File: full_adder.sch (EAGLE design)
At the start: 90 parts, among them U1001 FDS6892A, U1002 FDS6892A, U1003 FDS6892A, U101 ATTINY45-20P, U201 CD4052BE, U202 CD4052BE, U203 CD4052BE, U401 KM28C65A-20, U501 74HC4051N,652, U601 NE555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

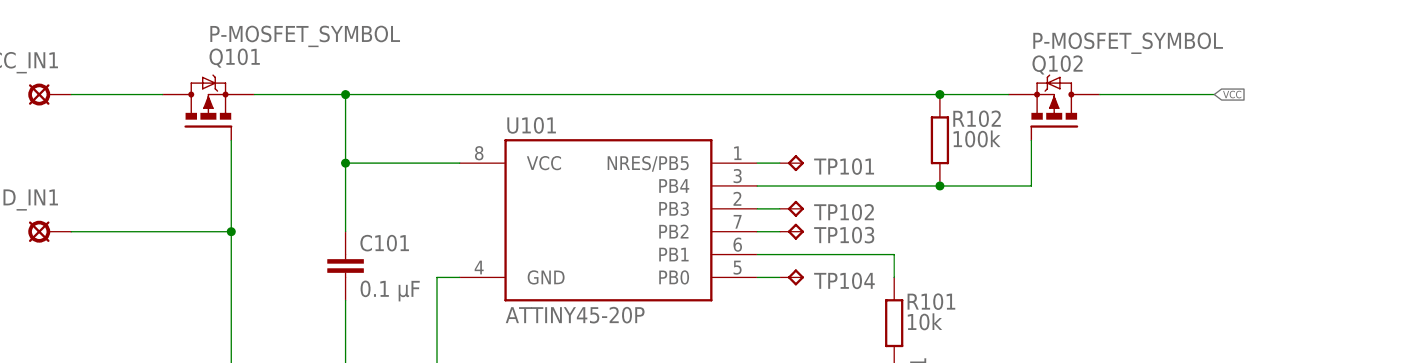
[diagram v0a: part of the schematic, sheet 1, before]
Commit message: p-channel footprint
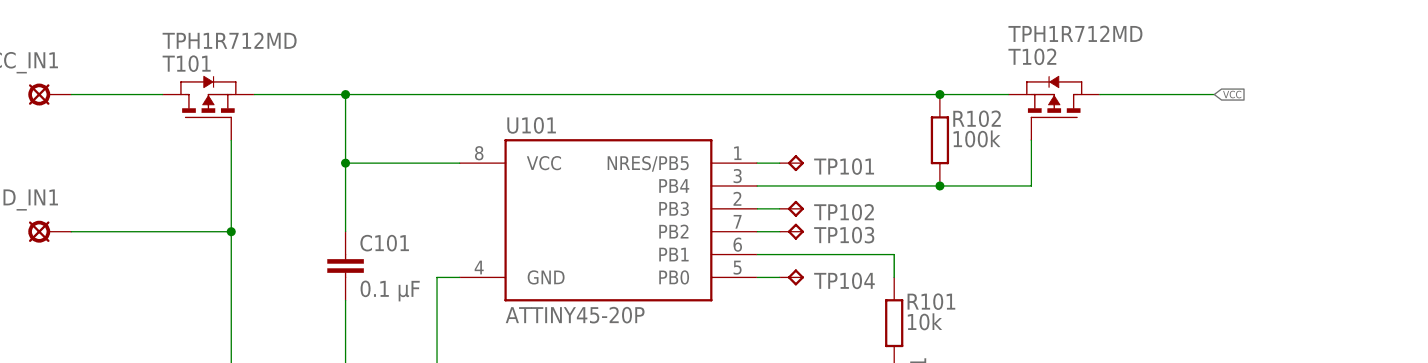
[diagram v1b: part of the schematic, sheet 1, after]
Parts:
- added T101, T102: TPH1R712MD, SamacSys_Parts:TPH1R712MD
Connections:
- net GND: now also T101.G
- net N$41: now also T101.D
- net N$42: now also T101.S, T102.S
- net N$43: now also T102.G
- net VCC: now also T102.D
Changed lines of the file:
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@@
 <part name="GND_IN1" library="solpad" library_urn="urn:adsk.eagle:library:364" deviceset="LSP11" device="" package3d_urn="urn:adsk.eagle:package:26502/1"/>
 <part name="GND40" library="supply1" library_urn="urn:adsk.eagle:library:371" deviceset="GND" device=""/>
-<part name="Q101" library="transistor-power" library_urn="urn:adsk.eagle:library:400" deviceset="P-MOSFET_SYMBOL" device=""/>
 <part name="U101" library="_hhn_attiny25_45_85" deviceset="ATTINY45*" device="P" technology="-20"/>
 <part name="GND52" library="supply1" library_urn="urn:adsk.eagle:library:371" deviceset="GND" device=""/>
@@
 <part name="TP103" library="testpad" library_urn="urn:adsk.eagle:library:385" deviceset="TP" device="B2,54" package3d_urn="urn:adsk.eagle:package:27948/1"/>
 <part name="TP104" library="testpad" library_urn="urn:adsk.eagle:library:385" deviceset="TP" device="B2,54" package3d_urn="urn:adsk.eagle:package:27948/1"/>
-<part name="Q102" library="transistor-power" library_urn="urn:adsk.eagle:library:400" deviceset="P-MOSFET_SYMBOL" device=""/>
+<part name="T102" library="SamacSys_Parts" deviceset="TPH1R712MD" device=""/>
+<part name="T101" library="SamacSys_Parts" deviceset="TPH1R712MD" device=""/>
 </parts>
 <sheets>
@@
 <attribute name="VALUE" x="307.34" y="180.34" size="1.778" layer="96"/>
 </instance>
-<instance part="Q101" gate="G$1" x="307.34" y="220.98" smashed="yes" rot="MR90">
-<attribute name="NAME" x="307.34" y="228.6" size="1.778" layer="95" rot="MR180"/>
-<attribute name="VALUE" x="307.34" y="231.14" size="1.778" layer="96" rot="MR180"/>
-</instance>
 <instance part="U101" gate="G$1" x="350.52" y="210.82" smashed="yes">
 <attribute name="NAME" x="340.36" y="219.202" size="1.778" layer="95"/>
@@
 <attribute name="TP_SIGNAL_NAME" x="372.11" y="201.93" size="1.778" layer="97" rot="R270"/>
 </instance>
-<instance part="Q102" gate="G$1" x="401.32" y="220.98" smashed="yes" rot="R90">
-<attribute name="NAME" x="398.78" y="226.06" size="1.778" layer="95"/>
-<attribute name="VALUE" x="398.78" y="228.6" size="1.778" layer="96"/>
+<instance part="T102" gate="G$1" x="401.32" y="223.52" smashed="yes" rot="MR90">
+<attribute name="VALUE" x="396.24" y="231.14" size="1.778" layer="96" rot="MR180"/>
+<attribute name="NAME" x="396.24" y="228.6" size="1.778" layer="95" rot="MR180"/>
+</instance>
+<instance part="T101" gate="G$1" x="307.34" y="223.52" smashed="yes" rot="R90">
+<attribute name="VALUE" x="302.26" y="228.6" size="1.778" layer="96"/>
+<attribute name="NAME" x="302.26" y="226.06" size="1.778" layer="95"/>
 </instance>
 </instances>
@@
 <wire x1="406.4" y1="223.52" x2="419.1" y2="223.52" width="0.1524" layer="91"/>
 <label x="419.1" y="223.52" size="0.8128" layer="95" xref="yes"/>
+<pinref part="T102" gate="G$1" pin="D"/>
 </segment>
 </net>
@@
 <segment>
 <pinref part="GND_IN1" gate="1" pin="MP"/>
-<wire x1="309.88" y1="218.44" x2="309.88" y2="208.28" width="0.1524" layer="91"/>
 <wire x1="309.88" y1="208.28" x2="292.1" y2="208.28" width="0.1524" layer="91"/>
 <pinref part="GND40" gate="1" pin="GND"/>
 <wire x1="309.88" y1="185.42" x2="309.88" y2="208.28" width="0.1524" layer="91"/>
+<pinref part="T101" gate="G$1" pin="G"/>
+<wire x1="309.88" y1="218.44" x2="309.88" y2="208.28" width="0.1524" layer="91"/>
 <junction x="309.88" y="208.28"/>
 </segment>
@@
 </segment>
 </net>
-<net name="N$41" class="0">
-<segment>
-<pinref part="VCC_IN1" gate="1" pin="MP"/>
-<wire x1="292.1" y1="223.52" x2="302.26" y2="223.52" width="0.1524" layer="91"/>
-</segment>
-</net>
 <net name="N$42" class="0">
 <segment>
-<wire x1="312.42" y1="223.52" x2="322.58" y2="223.52" width="0.1524" layer="91"/>
 <pinref part="U101" gate="G$1" pin="VCC"/>
 <wire x1="322.58" y1="223.52" x2="322.58" y2="215.9" width="0.1524" layer="91"/>
 <wire x1="322.58" y1="215.9" x2="335.28" y2="215.9" width="0.1524" layer="91"/>
 <wire x1="322.58" y1="223.52" x2="388.62" y2="223.52" width="0.1524" layer="91"/>
-<junction x="322.58" y="223.52"/>
 <pinref part="C101" gate="G$1" pin="1"/>
 <wire x1="388.62" y1="223.52" x2="396.24" y2="223.52" width="0.1524" layer="91"/>
@@
 <pinref part="R102" gate="G$1" pin="2"/>
 <junction x="388.62" y="223.52"/>
+<pinref part="T101" gate="G$1" pin="S"/>
+<wire x1="312.42" y1="223.52" x2="322.58" y2="223.52" width="0.1524" layer="91"/>
+<junction x="322.58" y="223.52"/>
+<pinref part="T102" gate="G$1" pin="S"/>
 </segment>
 </net>
@@
 <pinref part="R102" gate="G$1" pin="1"/>
 <junction x="388.62" y="213.36"/>
+<pinref part="T102" gate="G$1" pin="G"/>
 </segment>
 </net>
@@
 </segment>
 </net>
+<net name="N$41" class="0">
+<segment>
+<pinref part="VCC_IN1" gate="1" pin="MP"/>
+<pinref part="T101" gate="G$1" pin="D"/>
+<wire x1="292.1" y1="223.52" x2="302.26" y2="223.52" width="0.1524" layer="91"/>
+</segment>
+</net>

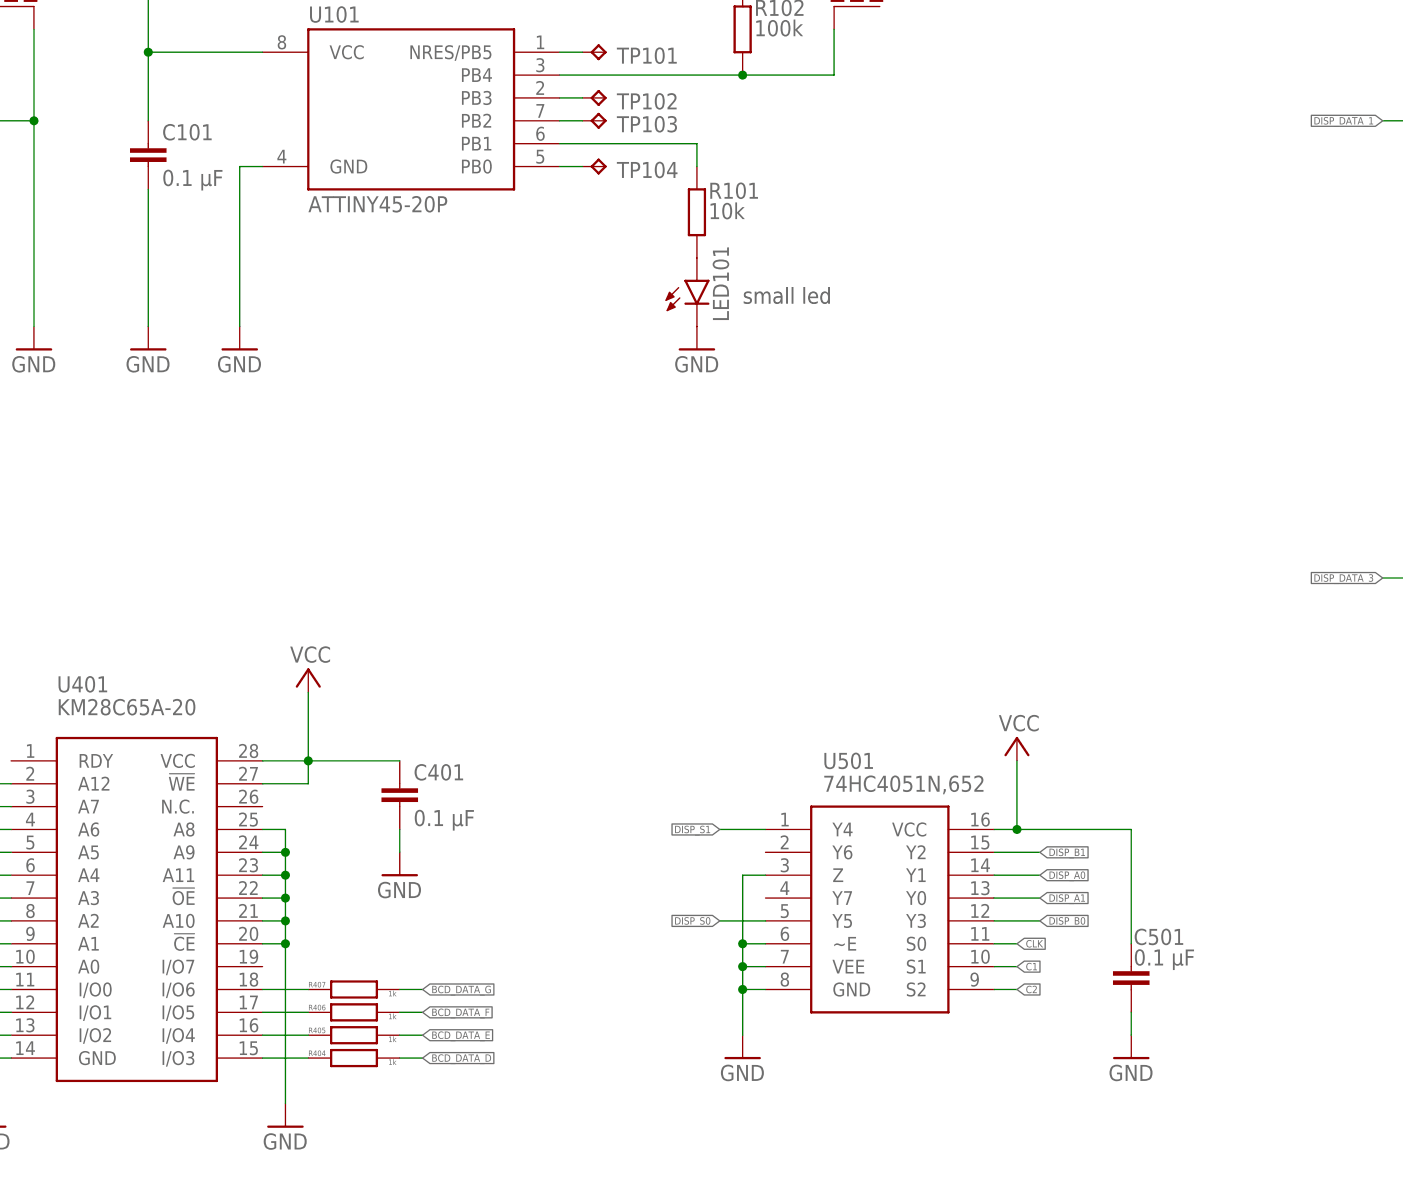
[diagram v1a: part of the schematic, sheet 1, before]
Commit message: swapped capacitor footprints
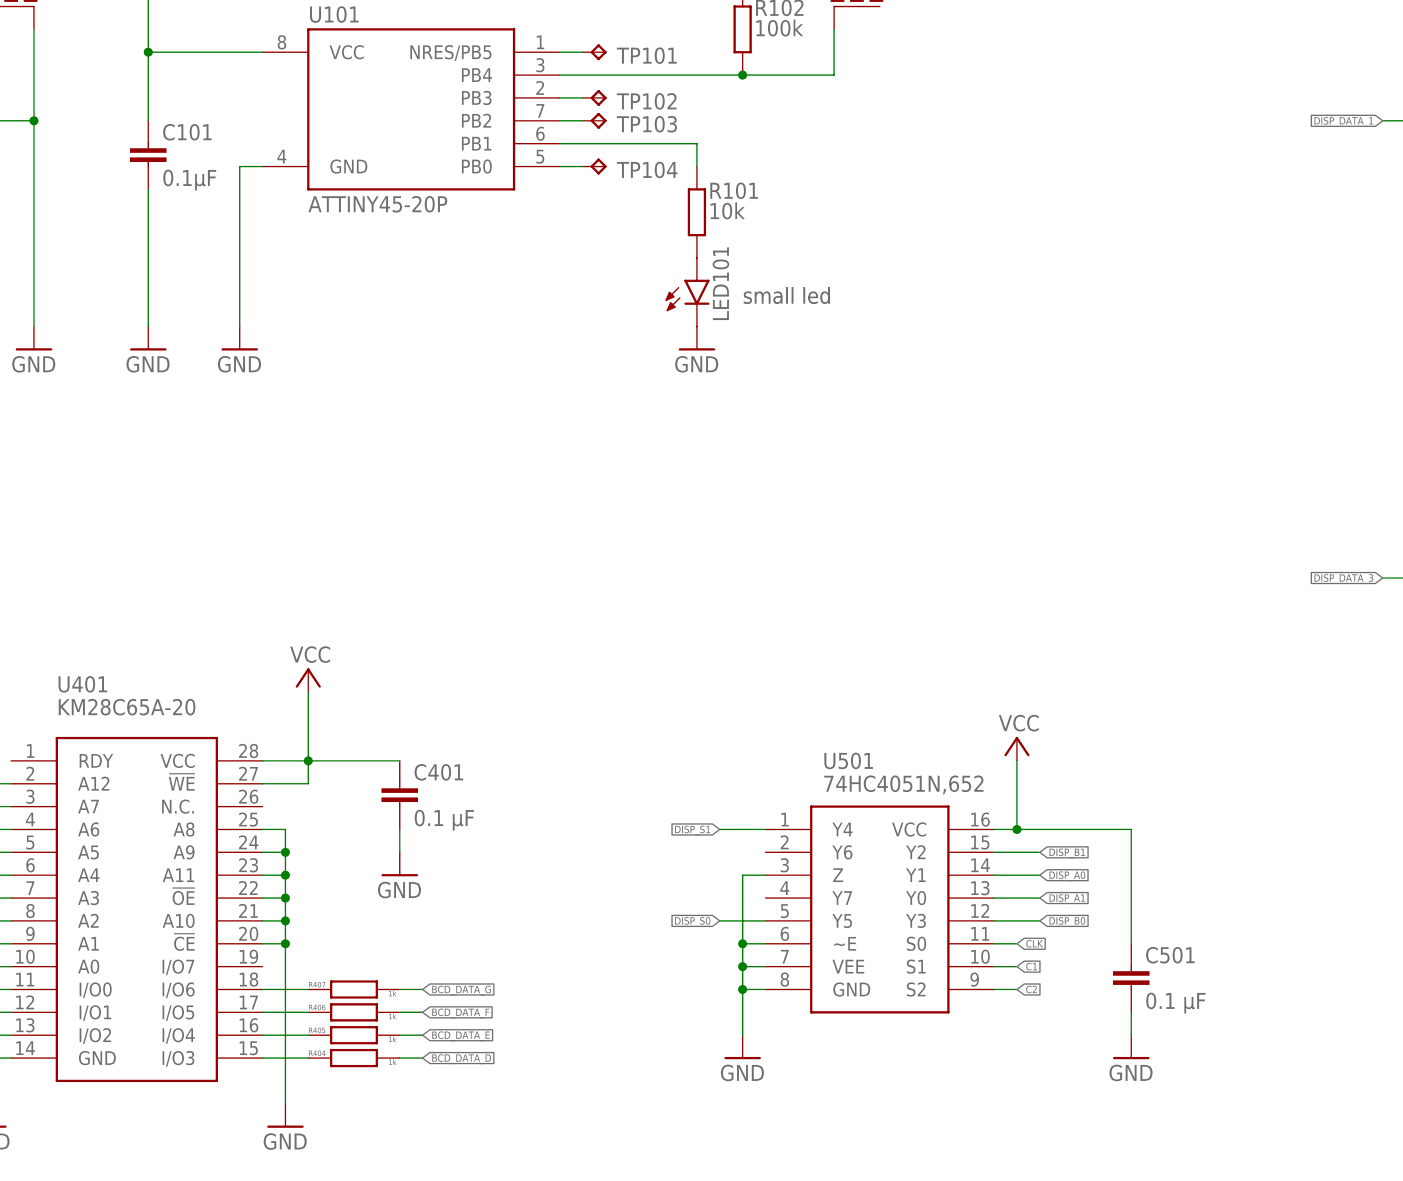
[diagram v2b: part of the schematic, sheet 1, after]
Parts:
- C101: value 0.1 µF -> 0.1µF; device rcl:C-EU025-024X044 -> rcl:C-EUC1206
- C201, C202, C203, C301, C302, C303, C304, C305, C401, C501, C601, C602, C603, C701: device rcl:C-EU025-024X044 -> rcl:C-EUC1206

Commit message: poti test pads
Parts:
- added POT_IN, POT_OUT, TP1: TPB2,54, testpad:TPB2,54
- C101: value 0.1µF -> 0.1 µF; device rcl:C-EUC1206 -> rcl:C-EU025-024X044
- C201, C202, C203, C301, C302, C303, C304, C305, C401, C501, C601, C602, C603, C701: device rcl:C-EUC1206 -> rcl:C-EU025-024X044
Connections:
- net N$14: now also POT_OUT.TP
- net N$15: now also POT_IN.TP
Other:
- moved on the sheet: R603

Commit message: fixed chaos
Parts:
- removed TP1: TPB2,54, testpad:TPB2,54
- C101: value 0.1 µF -> 0.1µF; device rcl:C-EU025-024X044 -> rcl:C-EUC1206
- C201, C202, C203, C301, C302, C303, C304, C305, C401, C501, C603, C701: device rcl:C-EU025-024X044 -> rcl:C-EUC1206
- C601: value 1 µF -> 1µF; device rcl:C-EU025-024X044 -> rcl:C-EU050-024X044
- C602: value 0.01 µF -> 0.01µF; device rcl:C-EU025-024X044 -> rcl:C-EU050-024X044
- renumbered POT_IN to POT_TP1, POT_OUT to POT_TP2

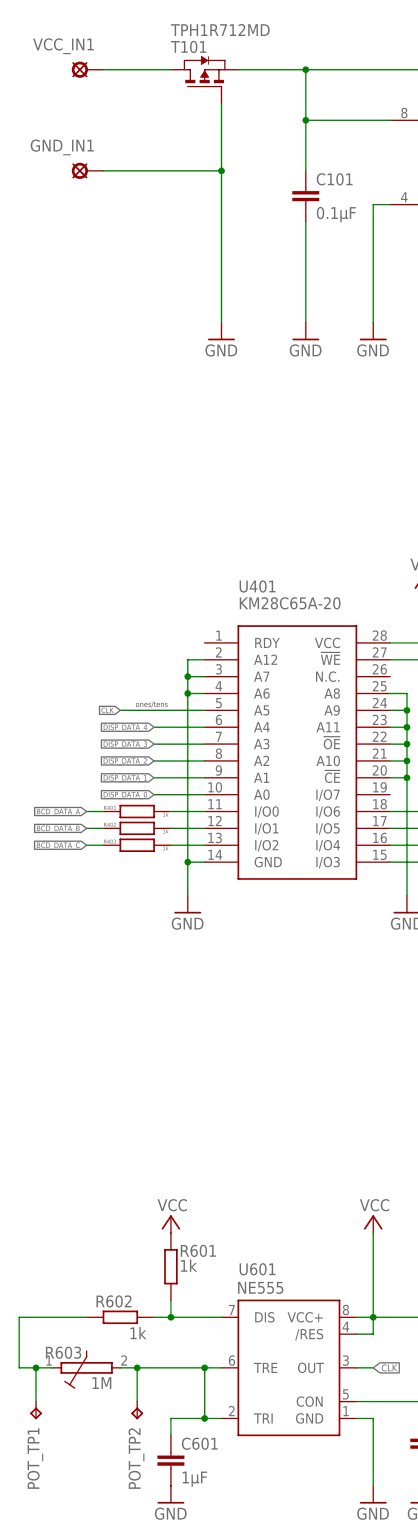
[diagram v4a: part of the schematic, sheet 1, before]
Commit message: swapped led footprints
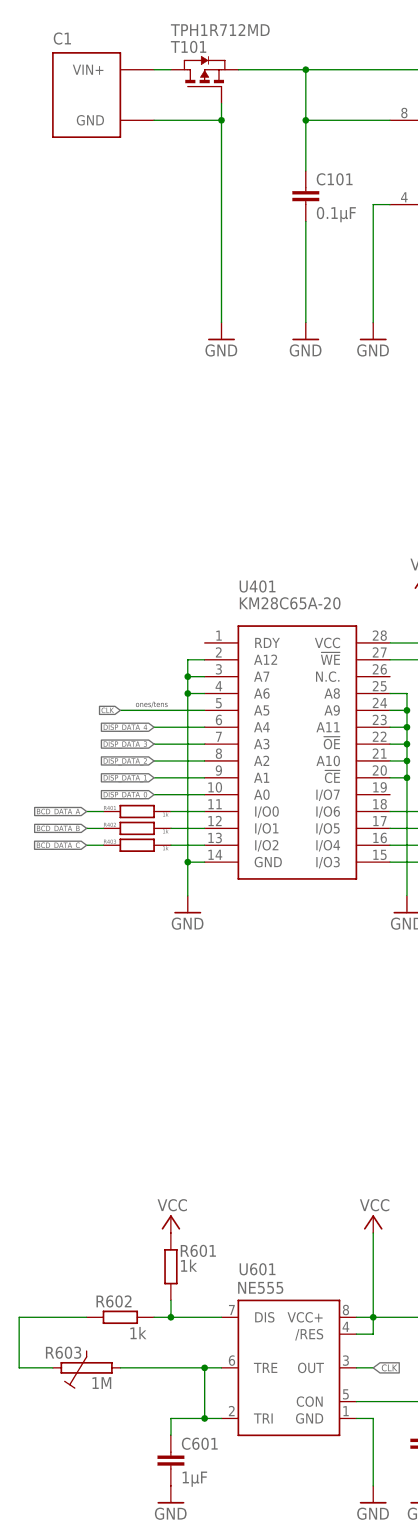
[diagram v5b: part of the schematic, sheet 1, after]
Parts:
- removed GND_IN1, VCC_IN1: LSP11, solpad:LSP11
- removed POT_TP1, POT_TP2: TPB2,54, testpad:TPB2,54
- added C1: BATTERY_CONNECTOR, custom:BATTERY_CONNECTOR
- LED1001, LED1002, LED1003, LED1004, LED1005, LED101, LED1101, LED1102, LED1103, LED1104, LED1105, LED1106, LED1107, LED1108: device led:LED5MM -> led:LED3MM
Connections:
- net GND: now also C1.GND; no longer GND_IN1.MP
- net N$14: no longer POT_TP2.TP
- net N$15: no longer POT_TP1.TP
- net N$41: now also C1.VIN+; no longer VCC_IN1.MP

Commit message: Components placed
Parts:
- U101: value ATTINY45-20P -> ATTINY85
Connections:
- new net N$45: R401.2, U401.I/O0
- new net N$46: R402.2, U401.I/O1
- new net N$47: R403.2, U401.I/O2
- new net N$48: R407.1, U401.I/O6
- new net N$49: R406.1, U401.I/O5
- new net N$50: R405.1, U401.I/O4
- new net N$51: R404.1, U401.I/O3
- net BCD_DATA_A: no longer R401.2, U401.I/O0
- net BCD_DATA_B: no longer R402.2, U401.I/O1
- net BCD_DATA_C: no longer R403.2, U401.I/O2
- net BCD_DATA_D: no longer R404.1, U401.I/O3
- net BCD_DATA_E: no longer R405.1, U401.I/O4
- net BCD_DATA_F: no longer R406.1, U401.I/O5
- net BCD_DATA_G: no longer R407.1, U401.I/O6

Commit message: routing v1 done
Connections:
- new net N$52: U701.1!Q, U701.1D
- net C1: no longer U701.1!Q, U701.1D
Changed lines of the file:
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@@
 <net name="C1" class="0">
-<segment>
-<pinref part="U701" gate="G$1" pin="1D"/>
-<wire x1="396.24" y1="33.02" x2="393.7" y2="33.02" width="0.1524" layer="91"/>
-<wire x1="393.7" y1="33.02" x2="393.7" y2="22.86" width="0.1524" layer="91"/>
-<pinref part="U701" gate="G$1" pin="1!Q"/>
-<wire x1="393.7" y1="22.86" x2="396.24" y2="22.86" width="0.1524" layer="91"/>
-</segment>
 <segment>
 <pinref part="U701" gate="G$1" pin="2CLK"/>
@@
 </segment>
 </net>
+<net name="N$52" class="0">
+<segment>
+<pinref part="U701" gate="G$1" pin="1D"/>
+<wire x1="396.24" y1="33.02" x2="393.7" y2="33.02" width="0.1524" layer="91"/>
+<wire x1="393.7" y1="33.02" x2="393.7" y2="22.86" width="0.1524" layer="91"/>
+<pinref part="U701" gate="G$1" pin="1!Q"/>
+<wire x1="393.7" y1="22.86" x2="396.24" y2="22.86" width="0.1524" layer="91"/>
+</segment>
+</net>
